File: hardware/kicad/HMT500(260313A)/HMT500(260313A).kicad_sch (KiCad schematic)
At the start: 0 parts

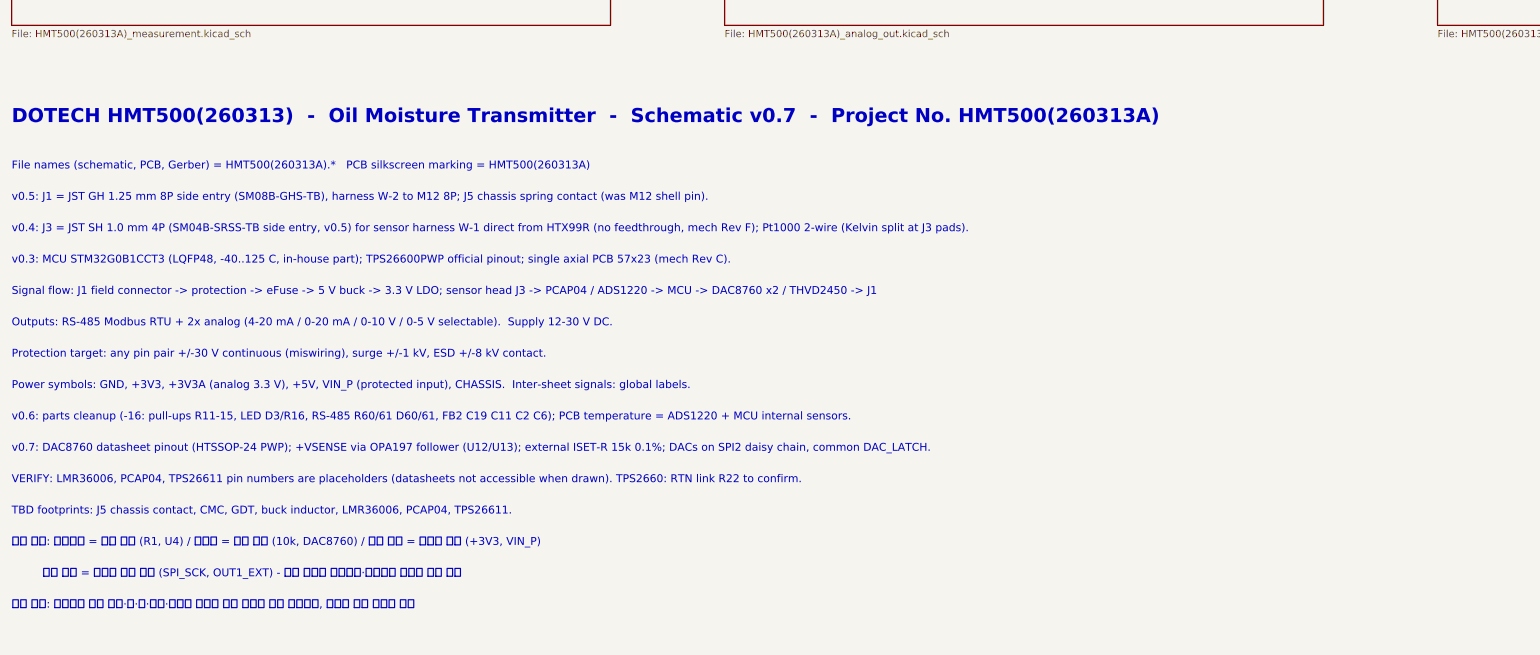
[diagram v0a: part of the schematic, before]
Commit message: Schematic v0.8: apply datasheet review A-O (HMT500(260313A))
- Real pinouts from manufacturer datasheets: LMR36006BRNXR (RNX-12),
  TPS26611DDFR (SOT-23-8), PCAP04 (QFN24); TPS2660 PowerPAD = RTN
- TPS2660: RTN isolated from GND (R22, R7 removed); R5/R6/C4/MODE on
  EF_RTN; R6 80.6k (149 mA); R5 41.2k -> OVP 29 V, supply 12-28 V so
  TPS26611 +Vs stays <= 30 V
- DAC SPI: per-DAC SCLK gating (74LVC2G32, SPI2 mode 3, LATCH1/2 on
  PB10/PB11) - daisy chain was removed in DAC8760 rev D
- DAC AVDD 10R series, ALARM wired-OR with 10k pull-up (PB6)
- Output TVS -> TVS3301 (stacked-pin two-terminal symbol)
- PCAP04 on dedicated SPI3 (PB3/4/5), VDD18 4.7uF, VDD33 10uF
- Buck per datasheet: L 15uH, COUT 2x22uF, CFF 20pF
- Shared VIN_P bulk (C53, C26 removed); PWR_FLT PB7; SGOOD -> PC6/PC7
- Parts list, circuit-design, decision log #26, review doc updated;
  netlist 74/74, 0 errors; tests pass

Co-Authored-By: Claude Opus 5.5 <noreply@anthropic.com>
Claude-Session: https://claude.ai/code/session_01JA2o8uJsqp9Vzsg4b665ev
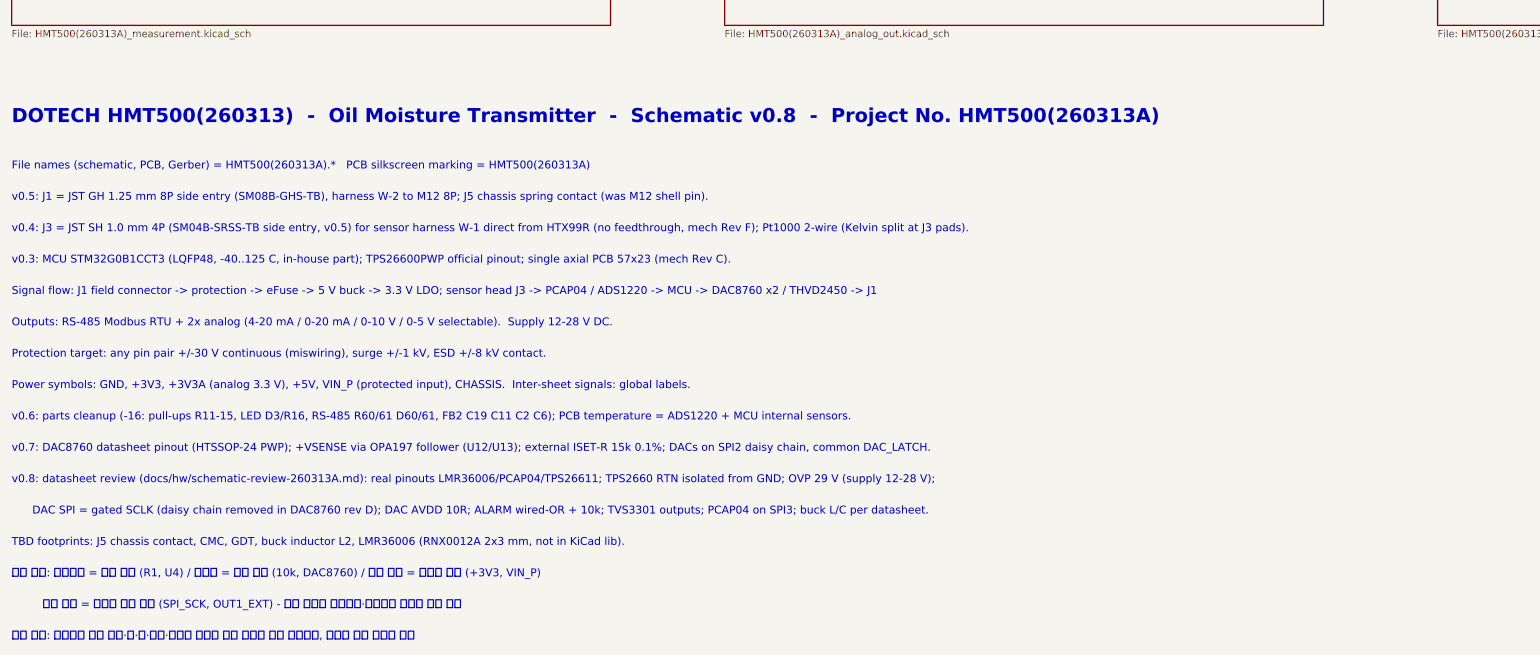
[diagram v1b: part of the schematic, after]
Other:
- note added: "DAC SPI = gated SCLK (daisy chain removed in DAC8760 rev D); DAC AVDD 10R; ALARM wired-OR + 10k; TVS3301 outputs; PCAP04 on SPI3; buck L/C per datasheet."
- note added: "DOTECH HMT500(260313) - Oil Moisture Transmitter - Schematic v0.8 - Project No. HMT500(260313A)"
- note added: "Outputs: RS-485 Modbus RTU + 2x analog (4-20 mA / 0-20 mA / 0-10 V / 0-5 V selectable). Supply 12-28 V DC."
- note added: "TBD footprints: J5 chassis contact, CMC, GDT, buck inductor L2, LMR36006 (RNX0012A 2x3 mm, not in KiCad lib)."
- note added: "v0.8: datasheet review (docs/hw/schematic-review-260313A.md): real pinouts LMR36006/PCAP04/TPS26611; TPS2660 RTN isolated from GND; OVP 29 V (supply 12-28 V);"
- note removed: "DOTECH HMT500(260313) - Oil Moisture Transmitter - Schematic v0.7 - Project No. HMT500(260313A)"
- note removed: "Outputs: RS-485 Modbus RTU + 2x analog (4-20 mA / 0-20 mA / 0-10 V / 0-5 V selectable). Supply 12-30 V DC."
- note removed: "TBD footprints: J5 chassis contact, CMC, GDT, buck inductor, LMR36006, PCAP04, TPS26611."
- note removed: "VERIFY: LMR36006, PCAP04, TPS26611 pin numbers are placeholders (datasheets not accessible when drawn). TPS2660: RTN link R22 to confirm."
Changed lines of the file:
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@@
 (kicad_sch (version 20230121) (generator eeschema) (paper "A3")
-(title_block (title "HMT500(260313A)  Top") (date "2026-09-29") (rev "0.7") (company "DOTECH Co., Ltd.") (comment 1 "Project No. HMT500(260313A)  -  HMT500(260313) oil moisture transmitter, RS-485 + 2x V/I output") (comment 2 "Design notes: docs/hw/circuit-design.md") (comment 3 "VERIFY=YES parts: pin numbers LMR36006/PCAP04/TPS26611; TPS2660 R22"))
+(title_block (title "HMT500(260313A)  Top") (date "2026-09-30") (rev "0.8") (company "DOTECH Co., Ltd.") (comment 1 "Project No. HMT500(260313A)  -  HMT500(260313) oil moisture transmitter") (comment 2 "Design notes: docs/hw/circuit-design.md") (comment 3 "Pinouts checked vs manufacturer datasheets 2026-09-30 (STM32: KiCad lib)"))
 (sheet (at 30.48 55.88) (size 106.68 45.72) (fields_autoplaced) (stroke (width 0.1524) (type solid)) (fill (color 0 0 0 0.0000)) (property "Sheetname" "1. Connector & input protection" (at 30.48 55.118 0) (effects (font (size 1.8 1.8) bold) (justify left bottom))) (property "Sheetfile" "HMT500(260313A)_connector.kicad_sch" (at 30.48 102.362 0) (effects (font (size 1.27 1.27)) (justify left top))) (instances (project "HMT500(260313A)" (path "/1ebb025b-11bd-5f7c-aaab-41e2a750e8b3" (page "2")))))
 (text "Field connector, 2-stage bidirectional TVS surge protection, chassis isolation" (at 33.02 78.74 0) (effects (font (size 1.4 1.4)) (justify left bottom)))
@@
 (sheet (at 284.48 132.08) (size 106.68 45.72) (fields_autoplaced) (stroke (width 0.1524) (type solid)) (fill (color 0 0 0 0.0000)) (property "Sheetname" "6. RS-485" (at 284.48 131.318 0) (effects (font (size 1.8 1.8) bold) (justify left bottom))) (property "Sheetfile" "HMT500(260313A)_rs485.kicad_sch" (at 284.48 178.562 0) (effects (font (size 1.27 1.27)) (justify left top))) (instances (project "HMT500(260313A)" (path "/1ebb025b-11bd-5f7c-aaab-41e2a750e8b3" (page "7")))))
 (text "THVD2450 +/-70V fault-protected transceiver" (at 287.02 154.94 0) (effects (font (size 1.4 1.4)) (justify left bottom)))
-(text "DOTECH HMT500(260313)  -  Oil Moisture Transmitter  -  Schematic v0.7  -  Project No. HMT500(260313A)" (at 30.48 195.58 0) (effects (font (size 2.5 2.5) bold) (justify left bottom)))
+(text "DOTECH HMT500(260313)  -  Oil Moisture Transmitter  -  Schematic v0.8  -  Project No. HMT500(260313A)" (at 30.48 195.58 0) (effects (font (size 2.5 2.5) bold) (justify left bottom)))
 (text "File names (schematic, PCB, Gerber) = HMT500(260313A).*   PCB silkscreen marking = HMT500(260313A)" (at 30.48 203.708 0) (effects (font (size 1.4 1.4)) (justify left bottom)))
 (text "v0.5: J1 = JST GH 1.25 mm 8P side entry (SM08B-GHS-TB), harness W-2 to M12 8P; J5 chassis spring contact (was M12 shell pin)." (at 30.48 209.296 0) (effects (font (size 1.4 1.4)) (justify left bottom)))
@@
 (text "v0.3: MCU STM32G0B1CCT3 (LQFP48, -40..125 C, in-house part); TPS26600PWP official pinout; single axial PCB 57x23 (mech Rev C)." (at 30.48 220.472 0) (effects (font (size 1.4 1.4)) (justify left bottom)))
 (text "Signal flow: J1 field connector -> protection -> eFuse -> 5 V buck -> 3.3 V LDO; sensor head J3 -> PCAP04 / ADS1220 -> MCU -> DAC8760 x2 / THVD2450 -> J1" (at 30.48 226.06 0) (effects (font (size 1.4 1.4)) (justify left bottom)))
-(text "Outputs: RS-485 Modbus RTU + 2x analog (4-20 mA / 0-20 mA / 0-10 V / 0-5 V selectable).  Supply 12-30 V DC." (at 30.48 231.648 0) (effects (font (size 1.4 1.4)) (justify left bottom)))
+(text "Outputs: RS-485 Modbus RTU + 2x analog (4-20 mA / 0-20 mA / 0-10 V / 0-5 V selectable).  Supply 12-28 V DC." (at 30.48 231.648 0) (effects (font (size 1.4 1.4)) (justify left bottom)))
 (text "Protection target: any pin pair +/-30 V continuous (miswiring), surge +/-1 kV, ESD +/-8 kV contact." (at 30.48 237.236 0) (effects (font (size 1.4 1.4)) (justify left bottom)))
 (text "Power symbols: GND, +3V3, +3V3A (analog 3.3 V), +5V, VIN_P (protected input), CHASSIS.  Inter-sheet signals: global labels." (at 30.48 242.824 0) (effects (font (size 1.4 1.4)) (justify left bottom)))
 (text "v0.6: parts cleanup (-16: pull-ups R11-15, LED D3/R16, RS-485 R60/61 D60/61, FB2 C19 C11 C2 C6); PCB temperature = ADS1220 + MCU internal sensors." (at 30.48 248.412 0) (effects (font (size 1.4 1.4)) (justify left bottom)))
 (text "v0.7: DAC8760 datasheet pinout (HTSSOP-24 PWP); +VSENSE via OPA197 follower (U12/U13); external ISET-R 15k 0.1%; DACs on SPI2 daisy chain, common DAC_LATCH." (at 30.48 254 0) (effects (font (size 1.4 1.4)) (justify left bottom)))
-(text "VERIFY: LMR36006, PCAP04, TPS26611 pin numbers are placeholders (datasheets not accessible when drawn). TPS2660: RTN link R22 to confirm." (at 30.48 259.588 0) (effects (font (size 1.4 1.4)) (justify left bottom)))
-(text "TBD footprints: J5 chassis contact, CMC, GDT, buck inductor, LMR36006, PCAP04, TPS26611." (at 30.48 265.176 0) (effects (font (size 1.4 1.4)) (justify left bottom)))
-(text "표기 규칙: 부품번호 = 굵은 글자 (R1, U4) / 부품값 = 보통 글자 (10k, DAC8760) / 전원 네트 = 기울인 글자 (+3V3, VIN_P)" (at 30.48 270.764 0) (effects (font (face "NanumGothic") (size 1.4 1.4)) (justify left bottom)))
-(text "         신호 네트 = 테두리 있는 라벨 (SPI_SCK, OUT1_EXT) - 네트 이름은 부품번호·부품명과 겹치지 않게 지음" (at 30.48 276.352 0) (effects (font (face "NanumGothic") (size 1.4 1.4)) (justify left bottom)))
-(text "글자 겹침: 생성기가 부품 몸체·핀·선·라벨·메모와 겹치지 않는 자리에 자동 배치하고, 겹치면 생성 실패로 처리" (at 30.48 281.94 0) (effects (font (face "NanumGothic") (size 1.4 1.4)) (justify left bottom)))
+(text "v0.8: datasheet review (docs/hw/schematic-review-260313A.md): real pinouts LMR36006/PCAP04/TPS26611; TPS2660 RTN isolated from GND; OVP 29 V (supply 12-28 V);" (at 30.48 259.588 0) (effects (font (size 1.4 1.4)) (justify left bottom)))
+(text "      DAC SPI = gated SCLK (daisy chain removed in DAC8760 rev D); DAC AVDD 10R; ALARM wired-OR + 10k; TVS3301 outputs; PCAP04 on SPI3; buck L/C per datasheet." (at 30.48 265.176 0) (effects (font (size 1.4 1.4)) (justify left bottom)))
+(text "TBD footprints: J5 chassis contact, CMC, GDT, buck inductor L2, LMR36006 (RNX0012A 2x3 mm, not in KiCad lib)." (at 30.48 270.764 0) (effects (font (size 1.4 1.4)) (justify left bottom)))
+(text "표기 규칙: 부품번호 = 굵은 글자 (R1, U4) / 부품값 = 보통 글자 (10k, DAC8760) / 전원 네트 = 기울인 글자 (+3V3, VIN_P)" (at 30.48 276.352 0) (effects (font (face "NanumGothic") (size 1.4 1.4)) (justify left bottom)))
+(text "         신호 네트 = 테두리 있는 라벨 (SPI_SCK, OUT1_EXT) - 네트 이름은 부품번호·부품명과 겹치지 않게 지음" (at 30.48 281.94 0) (effects (font (face "NanumGothic") (size 1.4 1.4)) (justify left bottom)))
+(text "글자 겹침: 생성기가 부품 몸체·핀·선·라벨·메모와 겹치지 않는 자리에 자동 배치하고, 겹치면 생성 실패로 처리" (at 30.48 287.528 0) (effects (font (face "NanumGothic") (size 1.4 1.4)) (justify left bottom)))
 (sheet_instances (path "/" (page "1")))
 )

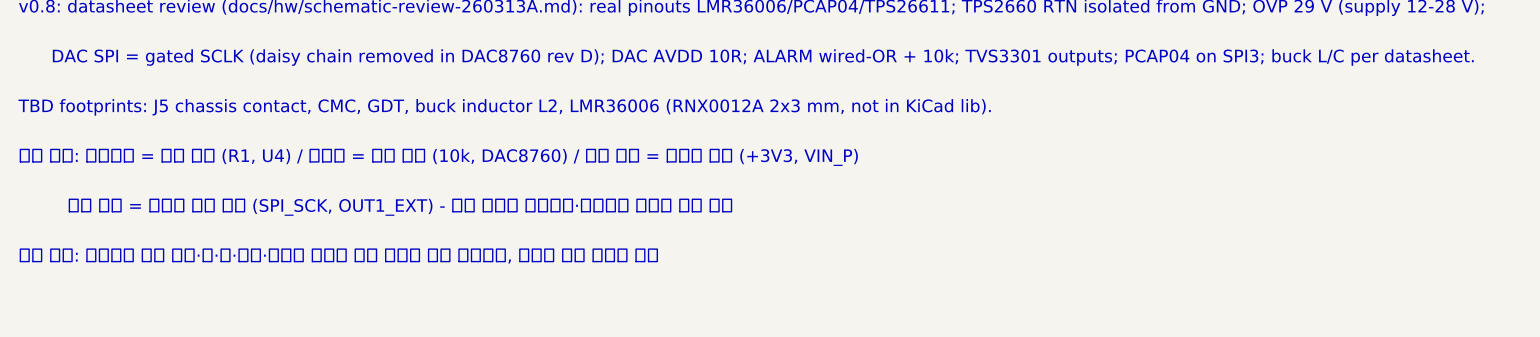
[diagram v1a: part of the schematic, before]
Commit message: Schematic: global label shape shows signal direction (driver = output, receiver = input)
Direction derived per net from pin types (output / tri-state / open-drain
drivers, MCU as driver when only inputs are on the other side); analog
and passive nets keep the plain shape, RS-485 bus bidirectional.
Legend line on the root sheet; test for key nets.

Co-Authored-By: Claude Opus 5.5 <noreply@anthropic.com>
Claude-Session: https://claude.ai/code/session_01JA2o8uJsqp9Vzsg4b665ev
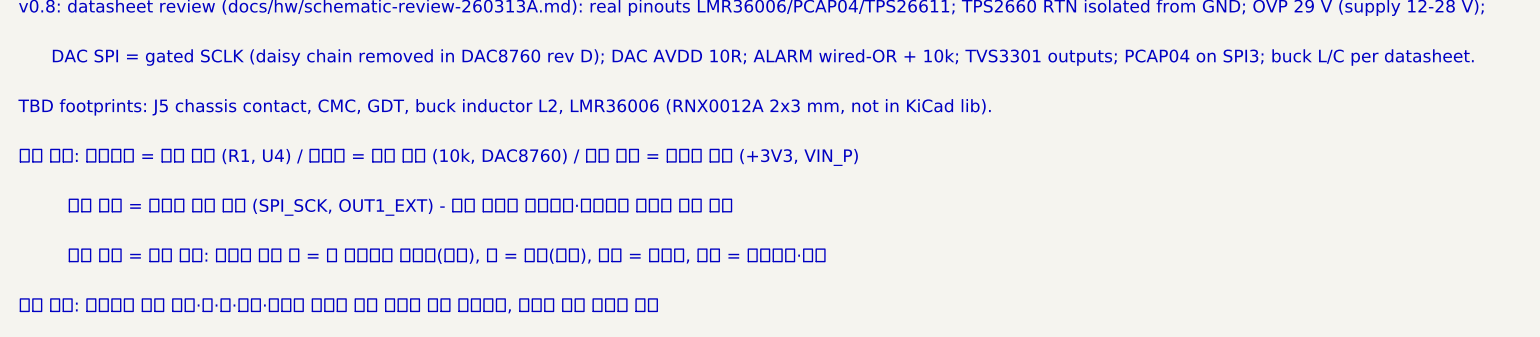
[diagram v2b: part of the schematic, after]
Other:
- note added: "라벨 모양 = 신호 방향: 뾰족한 쪽이 밖 = 이 시트에서 내보냄(출력), 안 = 받음(입력), 양쪽 = 양방향, 네모 = 아날로그·수동"
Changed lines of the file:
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@@
 (text "표기 규칙: 부품번호 = 굵은 글자 (R1, U4) / 부품값 = 보통 글자 (10k, DAC8760) / 전원 네트 = 기울인 글자 (+3V3, VIN_P)" (at 30.48 276.352 0) (effects (font (face "NanumGothic") (size 1.4 1.4)) (justify left bottom)))
 (text "         신호 네트 = 테두리 있는 라벨 (SPI_SCK, OUT1_EXT) - 네트 이름은 부품번호·부품명과 겹치지 않게 지음" (at 30.48 281.94 0) (effects (font (face "NanumGothic") (size 1.4 1.4)) (justify left bottom)))
-(text "글자 겹침: 생성기가 부품 몸체·핀·선·라벨·메모와 겹치지 않는 자리에 자동 배치하고, 겹치면 생성 실패로 처리" (at 30.48 287.528 0) (effects (font (face "NanumGothic") (size 1.4 1.4)) (justify left bottom)))
+(text "         라벨 모양 = 신호 방향: 뾰족한 쪽이 밖 = 이 시트에서 내보냄(출력), 안 = 받음(입력), 양쪽 = 양방향, 네모 = 아날로그·수동" (at 30.48 287.528 0) (effects (font (face "NanumGothic") (size 1.4 1.4)) (justify left bottom)))
+(text "글자 겹침: 생성기가 부품 몸체·핀·선·라벨·메모와 겹치지 않는 자리에 자동 배치하고, 겹치면 생성 실패로 처리" (at 30.48 293.116 0) (effects (font (face "NanumGothic") (size 1.4 1.4)) (justify left bottom)))
 (sheet_instances (path "/" (page "1")))
 )

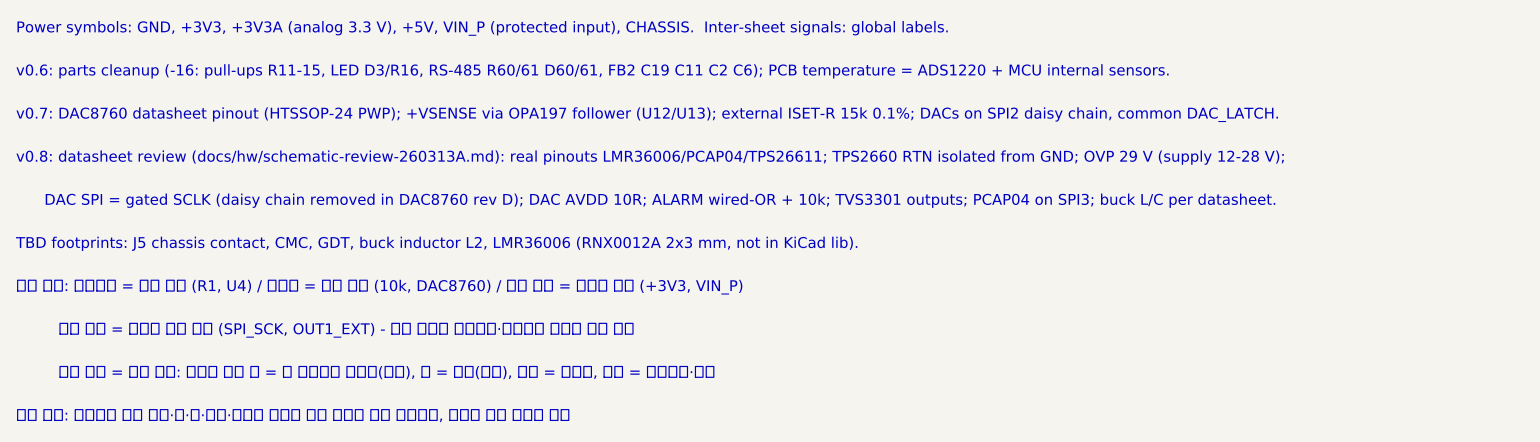
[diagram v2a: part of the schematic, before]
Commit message: Footprints and part numbers: no TBD left in the schematic
- Project footprint library hardware/kicad/lib/HMT500_260313A.pretty:
  KiCad 7.0.11 footprints + gen_footprints.py (LMR36006 RNX0012A from TI
  land pattern, Bourns 2035-xx-SM GDT, TVS3301 DRB with floating pad)
- GDT changed to 2-electrode Bourns 2035-23-SM-RPLF (2038 is 3-electrode)
- L1 Wurth WE-SL2 744222 (1 mH, 0.8 A); CMC pins renumbered to WE-SL2
  windings 1-4 / 2-3
- J5 Harwin S1941-46R, L2 Coilcraft XGL4030-153MEC, TPS26611 SOT-23-8,
  TPS2660 HTSSOP-16 footprint from 7.0.11
- R1 MMB02070C4708FB200, R30/R40 CRCW251210R0FKEGHP confirmed;
  R19 -> Vishay PLTT0603 0.02 % 5 ppm
- fp-lib-table written by the generator; netlist 74/74, tests pass

Co-Authored-By: Claude Opus 5.5 <noreply@anthropic.com>
Claude-Session: https://claude.ai/code/session_01JA2o8uJsqp9Vzsg4b665ev
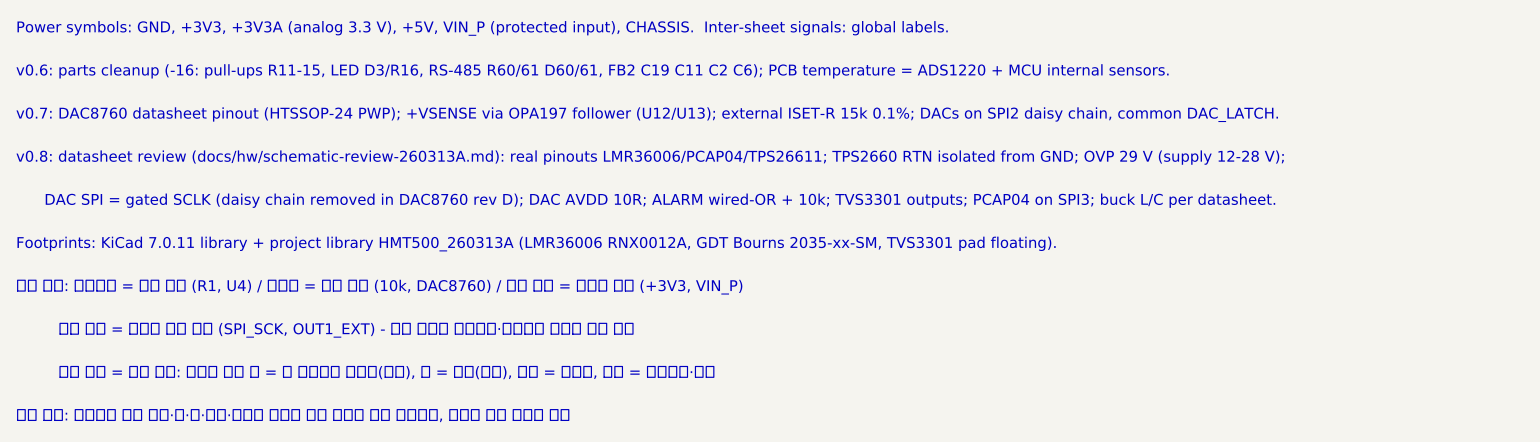
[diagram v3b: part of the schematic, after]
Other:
- note added: "Footprints: KiCad 7.0.11 library + project library HMT500_260313A (LMR36006 RNX0012A, GDT Bourns 2035-xx-SM, TVS3301 pad floating)."
- note removed: "TBD footprints: J5 chassis contact, CMC, GDT, buck inductor L2, LMR36006 (RNX0012A 2x3 mm, not in KiCad lib)."
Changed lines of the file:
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@@
 (text "v0.8: datasheet review (docs/hw/schematic-review-260313A.md): real pinouts LMR36006/PCAP04/TPS26611; TPS2660 RTN isolated from GND; OVP 29 V (supply 12-28 V);" (at 30.48 259.588 0) (effects (font (size 1.4 1.4)) (justify left bottom)))
 (text "      DAC SPI = gated SCLK (daisy chain removed in DAC8760 rev D); DAC AVDD 10R; ALARM wired-OR + 10k; TVS3301 outputs; PCAP04 on SPI3; buck L/C per datasheet." (at 30.48 265.176 0) (effects (font (size 1.4 1.4)) (justify left bottom)))
-(text "TBD footprints: J5 chassis contact, CMC, GDT, buck inductor L2, LMR36006 (RNX0012A 2x3 mm, not in KiCad lib)." (at 30.48 270.764 0) (effects (font (size 1.4 1.4)) (justify left bottom)))
+(text "Footprints: KiCad 7.0.11 library + project library HMT500_260313A (LMR36006 RNX0012A, GDT Bourns 2035-xx-SM, TVS3301 pad floating)." (at 30.48 270.764 0) (effects (font (size 1.4 1.4)) (justify left bottom)))
 (text "표기 규칙: 부품번호 = 굵은 글자 (R1, U4) / 부품값 = 보통 글자 (10k, DAC8760) / 전원 네트 = 기울인 글자 (+3V3, VIN_P)" (at 30.48 276.352 0) (effects (font (face "NanumGothic") (size 1.4 1.4)) (justify left bottom)))
 (text "         신호 네트 = 테두리 있는 라벨 (SPI_SCK, OUT1_EXT) - 네트 이름은 부품번호·부품명과 겹치지 않게 지음" (at 30.48 281.94 0) (effects (font (face "NanumGothic") (size 1.4 1.4)) (justify left bottom)))
